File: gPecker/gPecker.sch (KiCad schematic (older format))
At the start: 4 parts

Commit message: add kicad initial schematics..
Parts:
- removed C? (x2): 106,0805, symbol Device:C
- removed U?: RT9701, symbol Power_Management:RT9701
- added C15: 223,0603, symbol Device:C
- added C2: 105,0603, symbol Device:C
- added C5, C6: 105,0805, symbol Device:C
- added C7, C8: 104,0603, symbol Device:C
- added D1: PWR, symbol Device:LED
- added D2: SYS, symbol Device:LED
- added J1: USB_B_Mini, symbol Connector:USB_B_Mini
- added R1, R5: 510R,0603, symbol Device:R
- added R10: 4.7k,0603, symbol Device:R
- added R11, R9: 20R,0603, symbol Device:R
- added R2: 10K,0603, symbol Device:R
- added SW1: RESET, symbol Switch:SW_Push
- added U1: LDK130PU33R_DFN6, Package_DFN_QFN:DFN-6_1.3x1.2mm_P0.4mm, symbol Regulator_Linear:LDK130PU33R_DFN6
- gave numbers to parts that had none: 1
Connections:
- net Earth: now also C15.2, C2.2, C5.2, C6.2, C7.2, C8.2, D1.1 (K), J1.4 (ID), J1.5 (GND), J1.6 (Shield), SW1.1, U1.2 (GND)
- net at U2.2 (PC13): now also D2.1 (K)
- net RESET: now reaches U2.7 (NRST)
- net RESET: now also C2.1, R2.1, SW1.2
- new net: C15.1, U1.3 (BP)
- new net: J1.2 (D-), R9.2
- new net: J1.3 (D+), R11.2
- new net: D2.2 (A), R5.1
- new net: D1.2 (A), R1.1
- new net +3V3: C6.1, C8.1, R1.2, R2.2, R5.2, U1.1 (OUT)
- new net +5V: C5.1, C7.1, J1.1 (VBUS), R10.2, U1.4 (EN), U1.6 (IN)
- new net PA11: R9.1
- new net PA12: R10.1, R11.1
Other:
- moved on the sheet: U2

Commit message: correct some typos..
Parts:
- R10: value 4.7k,0603 -> 1.5k,0603
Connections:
- net +3V3: now also R10.2
- net +5V: no longer R10.2
- net Earth: no longer J1.4 (ID)
- net BOOT1: now reaches U2.22 (PB11)
- net BOOT0: now reaches U2.44 (BOOT0)
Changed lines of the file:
@@
 P 2050 1200
 F 0 "R10" H 1980 1154 50  0000 R CNN
-F 1 "4.7k,0603" H 1980 1245 50  0000 R CNN
+F 1 "1.5k,0603" H 1980 1245 50  0000 R CNN
 F 2 "" V 1980 1200 50  0001 C CNN
 F 3 "~" H 2050 1200 50  0001 C CNN
@@
 	-1   0    0    1
 $EndComp
-Wire Wire Line
-	1300 1700 1300 1950
-Wire Wire Line
-	1300 1950 1000 1950
-Connection ~ 1000 1950
-Wire Wire Line
-	1300 1600 1450 1600
-Wire Wire Line
-	1450 1500 1300 1500
 Text GLabel 2450 1500 2    50   Input ~ 0
 PA12
@@
 	4400 2850 4400 2950
 Wire Wire Line
-	1300 1300 1450 1300
-Wire Wire Line
-	1450 800  1450 1000
-Wire Wire Line
 	1750 1500 2050 1500
 Wire Wire Line
@@
 Wire Wire Line
 	2050 1500 2450 1500
-Wire Wire Line
-	2050 1050 2050 1000
-Wire Wire Line
-	2050 1000 1450 1000
-Connection ~ 1450 1000
-Wire Wire Line
-	1450 1000 1450 1300
 $Comp
 L Device:C C2
@@
 Wire Wire Line
 	1100 5400 1100 5450
+Text GLabel 7950 2700 0    50   Input ~ 0
+BOOT0
+Text GLabel 7950 4700 0    50   Input ~ 0
+BOOT1
+Wire Wire Line
+	8150 2700 7950 2700
+Wire Wire Line
+	8150 4700 7950 4700
+Wire Wire Line
+	1450 800  1450 1300
+$Comp
+L power:+3.3V #PWR?
+U 1 1 5C3D201E
+P 2050 800
+F 0 "#PWR?" H 2050 650 50  0001 C CNN
+F 1 "+3.3V" H 2065 973 50  0000 C CNN
+F 2 "" H 2050 800 50  0001 C CNN
+F 3 "" H 2050 800 50  0001 C CNN
+	1    2050 800
+	1    0    0    -1
+$EndComp
+Wire Wire Line
+	2050 1050 2050 800
+Wire Wire Line
+	1300 1600 1450 1600
+Wire Wire Line
+	1300 1500 1450 1500
+Wire Wire Line
+	1300 1300 1450 1300
 $EndSCHEMATC

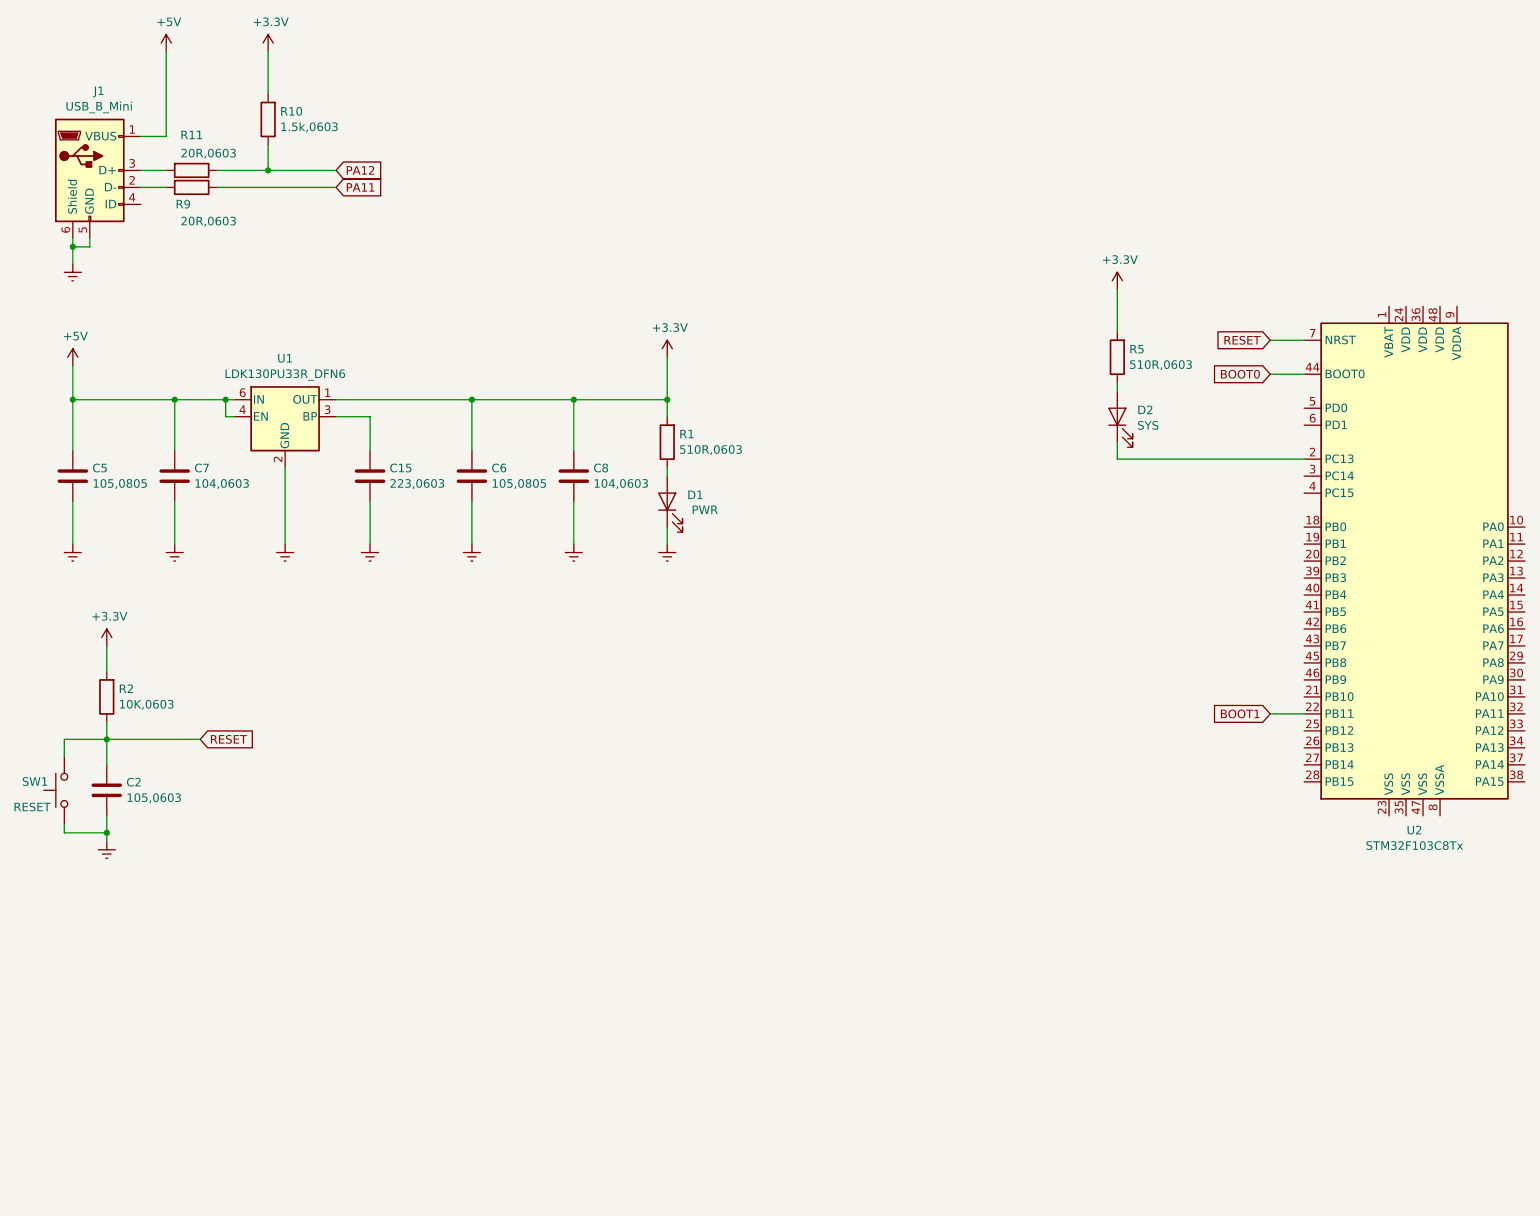
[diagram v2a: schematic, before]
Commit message: add SWD interface..
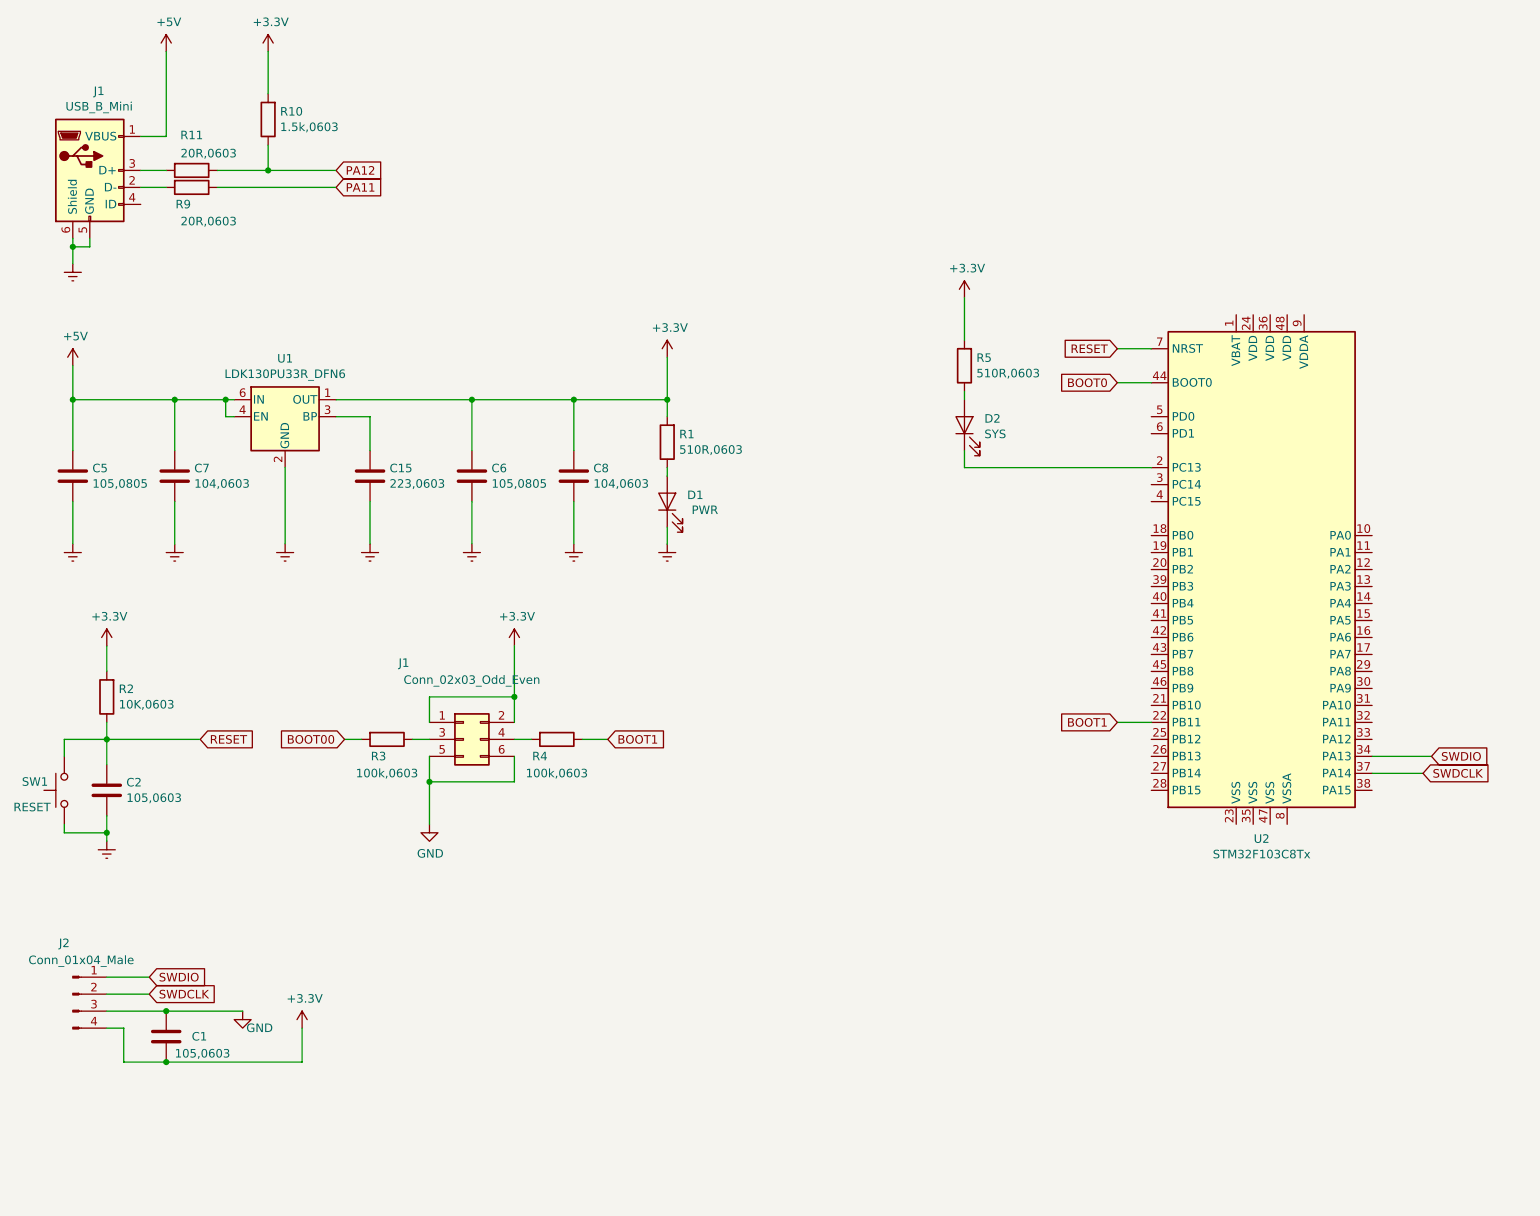
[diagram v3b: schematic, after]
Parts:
- added C1: 105,0603, symbol Device:C
- added J1: Conn_02x03_Odd_Even, symbol Connector_Generic:Conn_02x03_Odd_Even
- added J2: Conn_01x04_Male, symbol Connector:Conn_01x04_Male
- added R3, R4: 100k,0603, symbol Device:R
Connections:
- net +3V3: now also C1.2, J1.1 (Pin_1), J1.2 (Pin_2), J2.4 (Pin_4)
- net BOOT1: now also R4.1
- net SWDIO: now reaches U2.34 (PA13)
- net SWDIO: now also J2.1 (Pin_1)
- net SWDCLK: now reaches U2.37 (PA14)
- net SWDCLK: now also J2.2 (Pin_2)
- new net: J1.3 (Pin_3), R3.1
- new net: J1.4 (Pin_4), R4.2
- new net BOOT00: R3.2
- new net GND: C1.1, J1.5 (Pin_5), J1.6 (Pin_6), J2.3 (Pin_3)
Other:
- moved on the sheet: D2, R5, U2
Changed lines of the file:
@@
 L MCU_ST_STM32F1:STM32F103C8Tx U2
 U 1 1 5C3DBDD6
-P 8850 3800
-F 0 "U2" H 8800 2214 50  0000 C CNN
-F 1 "STM32F103C8Tx" H 8800 2123 50  0000 C CNN
-F 2 "Package_QFP:LQFP-48_7x7mm_P0.5mm" H 8250 2400 50  0001 R CNN
-F 3 "http://www.st.com/st-web-ui/static/active/en/resource/technical/document/datasheet/CD00161566.pdf" H 8850 3800 50  0001 C CNN
-	1    8850 3800
+P 7950 3850
+F 0 "U2" H 7900 2264 50  0000 C CNN
+F 1 "STM32F103C8Tx" H 7900 2173 50  0000 C CNN
+F 2 "Package_QFP:LQFP-48_7x7mm_P0.5mm" H 7350 2450 50  0001 R CNN
+F 3 "http://www.st.com/st-web-ui/static/active/en/resource/technical/document/datasheet/CD00161566.pdf" H 7950 3850 50  0001 C CNN
+	1    7950 3850
 	1    0    0    -1
 $EndComp
@@
 L power:+3.3V #PWR?
 U 1 1 5C3D4F78
-P 7050 2200
-F 0 "#PWR?" H 7050 2050 50  0001 C CNN
-F 1 "+3.3V" H 7065 2373 50  0000 C CNN
-F 2 "" H 7050 2200 50  0001 C CNN
-F 3 "" H 7050 2200 50  0001 C CNN
-	1    7050 2200
+P 6150 2250
+F 0 "#PWR?" H 6150 2100 50  0001 C CNN
+F 1 "+3.3V" H 6165 2423 50  0000 C CNN
+F 2 "" H 6150 2250 50  0001 C CNN
+F 3 "" H 6150 2250 50  0001 C CNN
+	1    6150 2250
 	1    0    0    -1
 $EndComp
@@
 L Device:LED D2
 U 1 1 5C3D4F7E
-P 7050 2950
-F 0 "D2" V 7088 2833 50  0000 R CNN
-F 1 "SYS" V 6997 2833 50  0000 R CNN
-F 2 "" H 7050 2950 50  0001 C CNN
-F 3 "~" H 7050 2950 50  0001 C CNN
-	1    7050 2950
+P 6150 3000
+F 0 "D2" V 6188 2883 50  0000 R CNN
+F 1 "SYS" V 6097 2883 50  0000 R CNN
+F 2 "" H 6150 3000 50  0001 C CNN
+F 3 "~" H 6150 3000 50  0001 C CNN
+	1    6150 3000
 	0    -1   -1   0
 $EndComp
@@
 L Device:R R5
 U 1 1 5C3D4F85
-P 7050 2600
-F 0 "R5" H 6980 2554 50  0000 R CNN
-F 1 "510R,0603" H 6980 2645 50  0000 R CNN
-F 2 "" V 6980 2600 50  0001 C CNN
-F 3 "~" H 7050 2600 50  0001 C CNN
-	1    7050 2600
+P 6150 2650
+F 0 "R5" H 6080 2604 50  0000 R CNN
+F 1 "510R,0603" H 6080 2695 50  0000 R CNN
+F 2 "" V 6080 2650 50  0001 C CNN
+F 3 "~" H 6150 2650 50  0001 C CNN
+	1    6150 2650
 	-1   0    0    1
 $EndComp
 Wire Wire Line
-	7050 2750 7050 2800
-Wire Wire Line
-	7050 2200 7050 2450
-Wire Wire Line
-	8150 3200 7050 3200
-Wire Wire Line
-	7050 3200 7050 3100
+	6150 2800 6150 2850
+Wire Wire Line
+	6150 2250 6150 2500
+Wire Wire Line
+	7250 3250 6150 3250
+Wire Wire Line
+	6150 3250 6150 3150
 Text GLabel 1650 4850 2    50   Input ~ 0
 RESET
@@
 Wire Wire Line
 	1100 4300 1100 4450
-Text GLabel 7950 2500 0    50   Input ~ 0
+Text GLabel 7050 2550 0    50   Input ~ 0
 RESET
 Wire Wire Line
-	8150 2500 7950 2500
+	7250 2550 7050 2550
 $Comp
 L power:+3.3V #PWR?
@@
 Wire Wire Line
 	1100 5400 1100 5450
-Text GLabel 7950 2700 0    50   Input ~ 0
+Text GLabel 7050 2750 0    50   Input ~ 0
 BOOT0
-Text GLabel 7950 4700 0    50   Input ~ 0
+Text GLabel 7050 4750 0    50   Input ~ 0
 BOOT1
 Wire Wire Line
-	8150 2700 7950 2700
-Wire Wire Line
-	8150 4700 7950 4700
+	7250 2750 7050 2750
+Wire Wire Line
+	7250 4750 7050 4750
 Wire Wire Line
 	1450 800  1450 1300
@@
 Wire Wire Line
 	1300 1300 1450 1300
+$Comp
+L Connector_Generic:Conn_02x03_Odd_Even J1
+U 1 1 5C3D9BBE
+P 3200 4850
+F 0 "J1" H 2850 5300 50  0000 C CNN
+F 1 "Conn_02x03_Odd_Even" H 3250 5200 50  0000 C CNN
+F 2 "" H 3200 4850 50  0001 C CNN
+F 3 "~" H 3200 4850 50  0001 C CNN
+	1    3200 4850
+	1    0    0    -1
+$EndComp
+Wire Wire Line
+	3000 4950 3000 5100
+Wire Wire Line
+	3000 5100 3500 5100
+Wire Wire Line
+	3500 5100 3500 4950
+$Comp
+L power:GND #PWR?
+U 1 1 5C3DB3D3
+P 3000 5350
+F 0 "#PWR?" H 3000 5100 50  0001 C CNN
+F 1 "GND" H 3005 5177 50  0000 C CNN
+F 2 "" H 3000 5350 50  0001 C CNN
+F 3 "" H 3000 5350 50  0001 C CNN
+	1    3000 5350
+	1    0    0    -1
+$EndComp
+Wire Wire Line
+	3000 4600 3500 4600
+$Comp
+L power:+3.3V #PWR?
+U 1 1 5C3DD3E8
+P 3500 4300
+F 0 "#PWR?" H 3500 4150 50  0001 C CNN
+F 1 "+3.3V" H 3515 4473 50  0000 C CNN
+F 2 "" H 3500 4300 50  0001 C CNN
+F 3 "" H 3500 4300 50  0001 C CNN
+	1    3500 4300
+	1    0    0    -1
+$EndComp
+Wire Wire Line
+	3500 4300 3500 4600
+$Comp
+L Device:R R3
+U 1 1 5C3E0AFE
+P 2750 4850
+F 0 "R3" V 2850 4800 50  0000 C CNN
+F 1 "100k,0603" V 2950 4850 50  0000 C CNN
+F 2 "" V 2680 4850 50  0001 C CNN
+F 3 "~" H 2750 4850 50  0001 C CNN
+	1    2750 4850
+	0    1    1    0
+$EndComp
+$Comp
+L Device:R R4
+U 1 1 5C3E1C70
+P 3750 4850
+F 0 "R4" V 3850 4750 50  0000 C CNN
+F 1 "100k,0603" V 3950 4850 50  0000 C CNN
+F 2 "" V 3680 4850 50  0001 C CNN
+F 3 "~" H 3750 4850 50  0001 C CNN
+	1    3750 4850
+	0    1    1    0
+$EndComp
+Wire Wire Line
+	2900 4850 3000 4850
+Wire Wire Line
+	3600 4850 3500 4850
+Text GLabel 2500 4850 0    50   Input ~ 0
+BOOT00
+Text GLabel 4050 4850 2    50   Input ~ 0
+BOOT1
+Wire Wire Line
+	4050 4850 3900 4850
+Wire Wire Line
+	2600 4850 2500 4850
+Wire Wire Line
+	3500 4750 3500 4600
+Connection ~ 3500 4600
+Wire Wire Line
+	3000 4750 3000 4600
+Wire Wire Line
+	3000 5350 3000 5100
+Connection ~ 3000 5100
+$Comp
+L Connector:Conn_01x04_Male J2
+U 1 1 5C3F6859
+P 900 6350
+F 0 "J2" H 850 6650 50  0000 C CNN
+F 1 "Conn_01x04_Male" H 950 6550 50  0000 C CNN
+F 2 "" H 900 6350 50  0001 C CNN
+F 3 "~" H 900 6350 50  0001 C CNN
+	1    900  6350
+	1    0    0    -1
+$EndComp
+$Comp
+L power:GND #PWR?
+U 1 1 5C3F6DCA
+P 1900 6450
+F 0 "#PWR?" H 1900 6200 50  0001 C CNN
+F 1 "GND" H 2000 6350 50  0000 C CNN
+F 2 "" H 1900 6450 50  0001 C CNN
+F 3 "" H 1900 6450 50  0001 C CNN
+	1    1900 6450
+	1    0    0    -1
+$EndComp
+$Comp
+L power:+3.3V #PWR?
+U 1 1 5C3FBC46
+P 2250 6550
+F 0 "#PWR?" H 2250 6400 50  0001 C CNN
+F 1 "+3.3V" H 2265 6723 50  0000 C CNN
+F 2 "" H 2250 6550 50  0001 C CNN
+F 3 "" H 2250 6550 50  0001 C CNN
+	1    2250 6550
+	1    0    0    -1
+$EndComp
+Text GLabel 1350 6250 2    50   Input ~ 0
+SWDIO
+Text GLabel 1350 6350 2    50   Input ~ 0
+SWDCLK
+$Comp
+L Device:C C1
+U 1 1 5C4017FB
+P 1450 6600
+F 0 "C1" H 1600 6600 50  0000 L CNN
+F 1 "105,0603" H 1500 6500 50  0000 L CNN
+F 2 "" H 1488 6450 50  0001 C CNN
+F 3 "~" H 1450 6600 50  0001 C CNN
+	1    1450 6600
+	1    0    0    -1
+$EndComp
+Wire Wire Line
+	1100 6250 1350 6250
+Wire Wire Line
+	1350 6350 1100 6350
+Wire Wire Line
+	2250 6750 2250 6550
+Wire Wire Line
+	1100 6450 1450 6450
+Wire Wire Line
+	1100 6550 1200 6550
+Wire Wire Line
+	1200 6550 1200 6750
+Wire Wire Line
+	1200 6750 1450 6750
+Wire Wire Line
+	1900 6450 1450 6450
+Connection ~ 1450 6450
+Wire Wire Line
+	2250 6750 1450 6750
+Connection ~ 1450 6750
+Text GLabel 8900 4950 2    50   Input ~ 0
+SWDIO
+Wire Wire Line
+	8900 4950 8550 4950
+Text GLabel 8850 5050 2    50   Input ~ 0
+SWDCLK
+Wire Wire Line
+	8850 5050 8550 5050
 $EndSCHEMATC

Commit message: correct typo..
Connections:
- net BOOT00 is gone; now on net BOOT0: R3.2
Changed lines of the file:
@@
 	3600 4850 3500 4850
 Text GLabel 2500 4850 0    50   Input ~ 0
-BOOT00
+BOOT0
 Text GLabel 4050 4850 2    50   Input ~ 0
 BOOT1
